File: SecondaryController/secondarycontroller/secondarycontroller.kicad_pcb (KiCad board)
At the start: 2 copper layers, 9 parts, among them J1 Receiver, J3 VIN, J4 APA102C, J5 I2C BUS, SW1 Calibrate, SW2 Reset

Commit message: Finished PCB Secondary
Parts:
- removed D1, D2: DIODE, Diode_THT:D_5W_P12.70mm_Horizontal
- added J2: Conn_01x07_Female, Connector_PinSocket_2.54mm:PinSocket_1x07_P2.54mm_Vertical, F.Cu at (175.3, 63.5)
- added XA1: Arduino_Uno_Shield, Arduino:Arduino_Uno_Shield, F.Cu at (144.9, 105.5)
- CF15: footprint Capacitor_THT:C_Rect_L41.5mm_W19.0mm_P37.50mm_MKS4 -> Capacitor_THT:C_Rect_L41.5mm_W13.0mm_P37.50mm_MKS4
- SW1, SW2: footprint Button_Switch_THT:SW_DIP_SPSTx01_Piano_10.8x4.1mm_W7.62mm_P2.54mm -> Button_Switch_THT:SW_PUSH_6mm
- moved J4 92.2 mm to (204.5, 71.1), turned to 180 degrees
- moved CF15 83.1 mm to (160.0, 94.0)
- moved SW2 67.2 mm to (147.3, 67.3)
- moved J5 58.4 mm to (149.9, 58.4), turned to 180 degrees
- moved J3 57.0 mm to (149.9, 94.0)
- moved J1 38.1 mm to (160.0, 72.4), turned to 180 degrees
- moved SW1 29.0 mm to (147.3, 78.7)
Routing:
- net Net-(CF15-Pad1): track 0.00 -> 156.2 mm
- net Net-(J2-Pad1): track 0.00 -> 72.0 mm
- net Net-(J3-Pad2): track 0.00 -> 47.4 mm
- net Net-(SW1-Pad1): track 0.00 -> 46.9 mm
- net Net-(SW2-Pad2): track 0.00 -> 41.1 mm
- net Net-(J4-Pad2): track 0.00 -> 25.5 mm
- net Net-(J1-Pad3): track 0.00 -> 22.3 mm
- net Net-(J5-Pad1): track 0.00 -> 21.0 mm
- net Net-(J4-Pad3): track 0.00 -> 20.1 mm
- net Net-(J5-Pad2): track 0.00 -> 17.0 mm
- net Net-(CF15-Pad2): track 0.00 -> 9.74 mm
- net Net-(J2-Pad3): track 0.00 -> 9.42 mm
- net Net-(J2-Pad4): track 0.00 -> 9.42 mm
- net Net-(J2-Pad5): track 0.00 -> 9.27 mm
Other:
- net class Default: trace_width 0.25 -> 1.5

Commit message: secondary as done
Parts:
- moved J1 12.9 mm to (172.1, 67.9), turned to 270 degrees
- moved J3 12.7 mm to (149.2, 81.3)
- moved SW2 9.86 mm to (156.8, 69.8)
- moved SW1 9.71 mm to (156.8, 80.6)
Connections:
- XA1 pad GND1: (no net) -> Net-(XA1-PadGND1)
- XA1 pad GND2: (no net) -> Net-(CF15-Pad1)
- XA1 pad GND3: (no net) -> Net-(XA1-PadGND3)
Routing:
- net Net-(CF15-Pad1): track 156.2 -> 223.5 mm
- net Net-(SW1-Pad1): track 46.9 -> 33.0 mm
- net Net-(J3-Pad2): track 47.4 -> 58.1 mm
- net Net-(SW2-Pad2): track 41.1 -> 34.6 mm
- net Net-(J1-Pad3): track 22.3 -> 17.1 mm
- net Net-(J5-Pad1): track 21.0 -> 19.1 mm
- net Net-(J5-Pad2): track 17.0 -> 15.5 mm
- added copper zone on B.Cu, net Net-(CF15-Pad1)
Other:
- board outline added: 69.2 x 59.1 mm

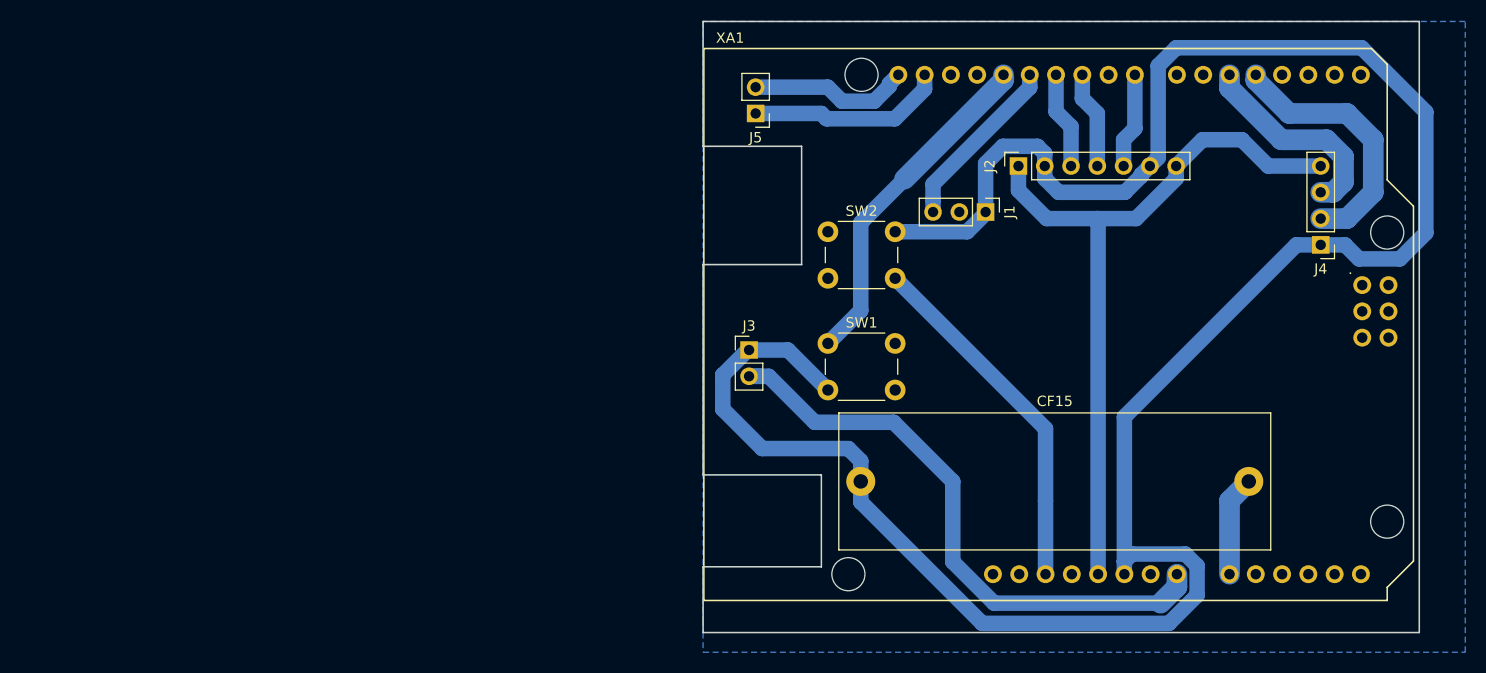
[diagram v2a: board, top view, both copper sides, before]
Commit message: new secondary controller pcb design
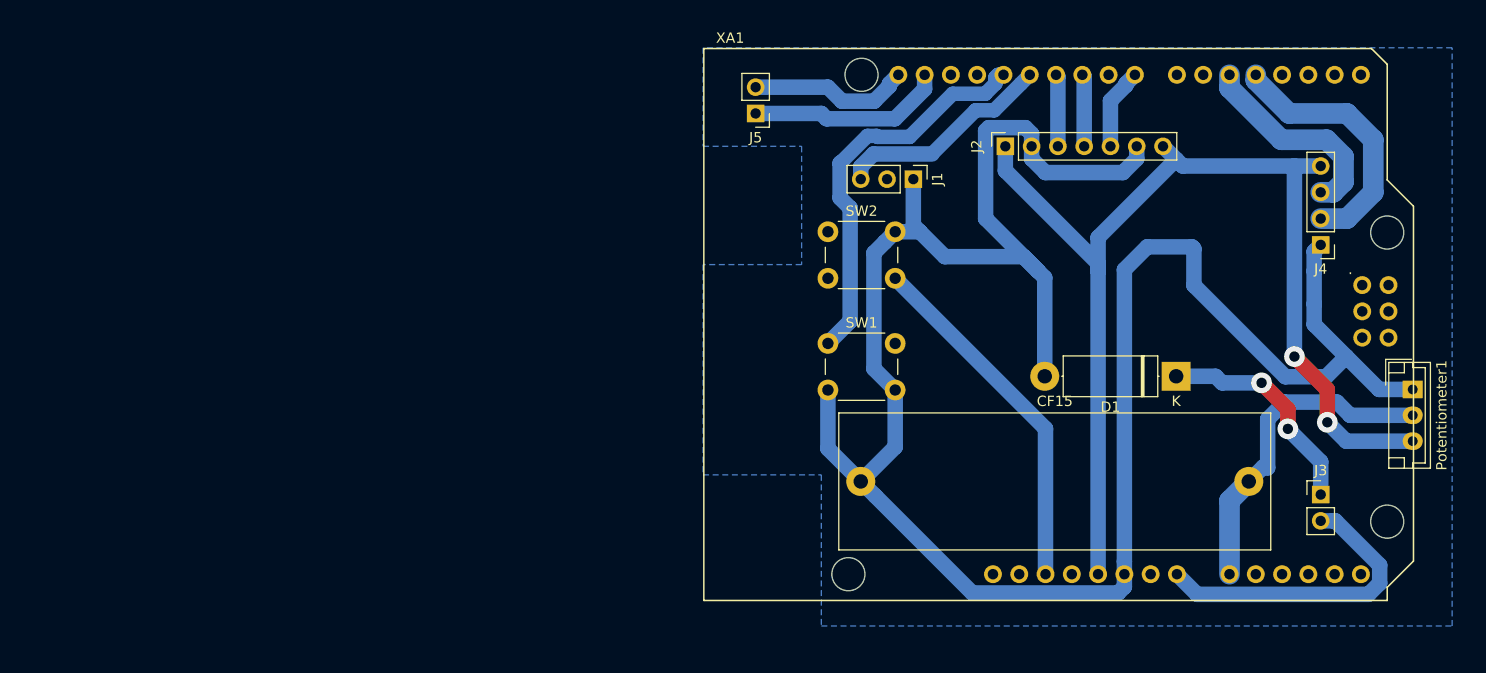
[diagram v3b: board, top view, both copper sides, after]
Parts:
- added D1: DIODE, Diode_THT:D_5W_P12.70mm_Horizontal, F.Cu at (190.5, 83.8)
- added Potentiometer1: Conn_01x03_Male, Connector_JST:JST_EH_B03B-EH-A_1x03_P2.50mm_Vertical, F.Cu at (213.4, 85.1)
- moved J3 57.0 mm to (204.5, 95.2)
- moved J1 7.67 mm to (165.1, 64.8)
- moved J2 2.29 mm to (174.0, 61.6)
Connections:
- J3 pad 1: Net-(CF15-Pad1) -> Net-(D1-Pad1)
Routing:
- net Net-(J2-Pad1): track 72.0 -> 110.8 mm, vias 0 -> 2
- net Net-(J3-Pad2): track 58.1 -> 30.1 mm
- net Net-(CF15-Pad2): track 9.74 -> 32.1 mm
- net Net-(D1-Pad1): track 0.00 -> 21.7 mm, vias 0 -> 2
- net Net-(CF15-Pad1): track 223.5 -> 215.2 mm
- net Net-(SW1-Pad1): track 33.0 -> 38.7 mm
- net Net-(J1-Pad3): track 17.1 -> 21.2 mm
- net Net-(J2-Pad3): track 9.42 -> 6.98 mm
- net Net-(J2-Pad4): track 9.42 -> 6.98 mm
- net Net-(J2-Pad5): track 9.27 -> 7.89 mm
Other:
- board outline removed
- net class Default: clearance 0.2 -> 0.3
- rule trace_clearance: 0.2 -> 0.3

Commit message: secondary better pcb design
Signed-off-by: Kai Boernert <kai-boernert@visiongamestudios.de>
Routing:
- net (no net): track 0.00 -> 50.0 mm
- net Net-(CF15-Pad1): track 215.2 -> 237.8 mm
- net Net-(J2-Pad1): track 110.8 -> 132.3 mm
- net Net-(SW1-Pad1): track 38.7 -> 59.4 mm
- net Net-(SW2-Pad2): track 34.6 -> 48.6 mm
- net Net-(CF15-Pad2): track 32.1 -> 42.1 mm
- net Net-(J3-Pad2): track 30.1 -> 33.1 mm
- net Net-(XA1-PadGND3): track 0.00 -> 2.54 mm
- net Net-(XA1-PadA3): track 0.00 -> 2.54 mm
- net Net-(XA1-PadA2): track 0.00 -> 2.54 mm
- net Net-(XA1-PadA1): track 0.00 -> 2.54 mm
- net Net-(XA1-PadD7): track 0.00 -> 2.50 mm
- net Net-(XA1-PadA4): track 0.00 -> 2.48 mm
- net Net-(XA1-PadD0): track 0.00 -> 2.39 mm
- net Net-(XA1-PadD6): track 0.00 -> 2.39 mm
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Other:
- net class Default: clearance 0.3 -> 0.1; trace_width 1.5 -> 1
- rule trace_clearance: 0.3 -> 0.1

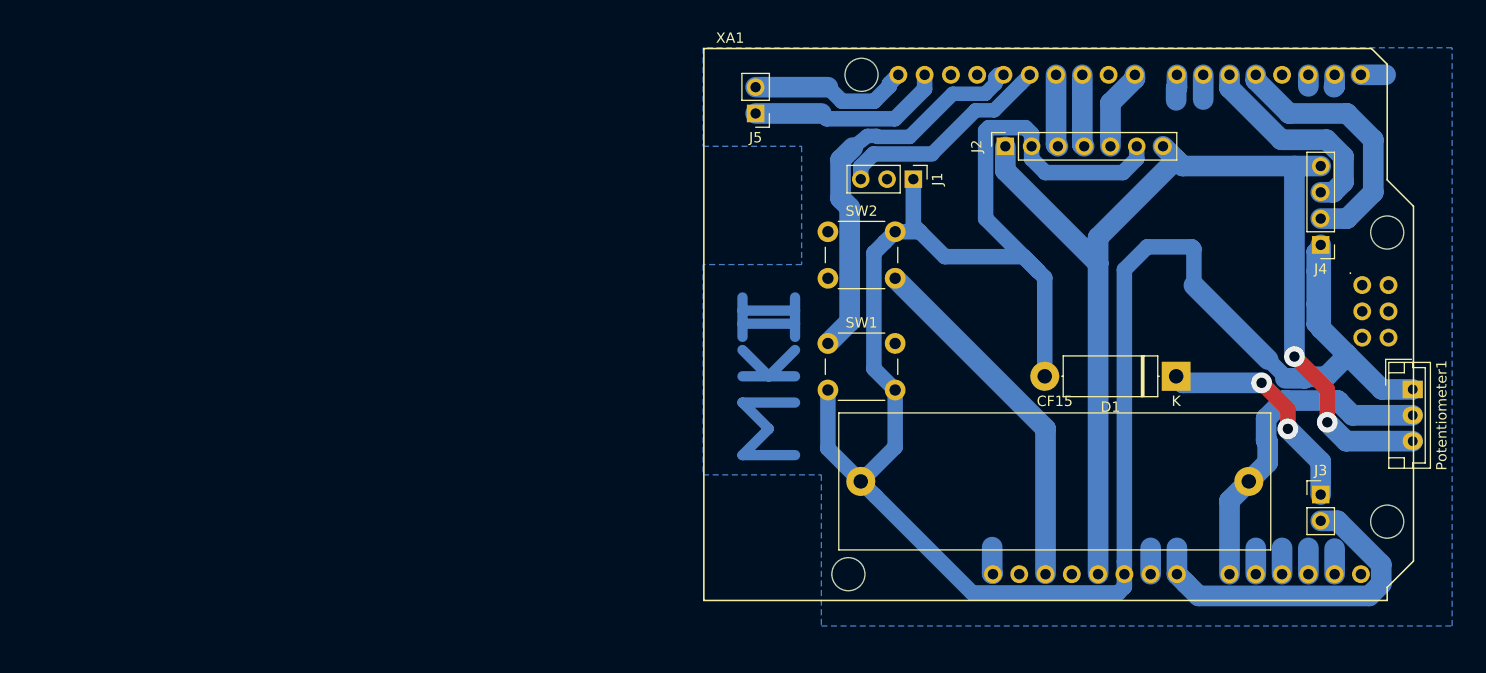
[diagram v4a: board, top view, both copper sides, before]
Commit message: secondary controller mk2
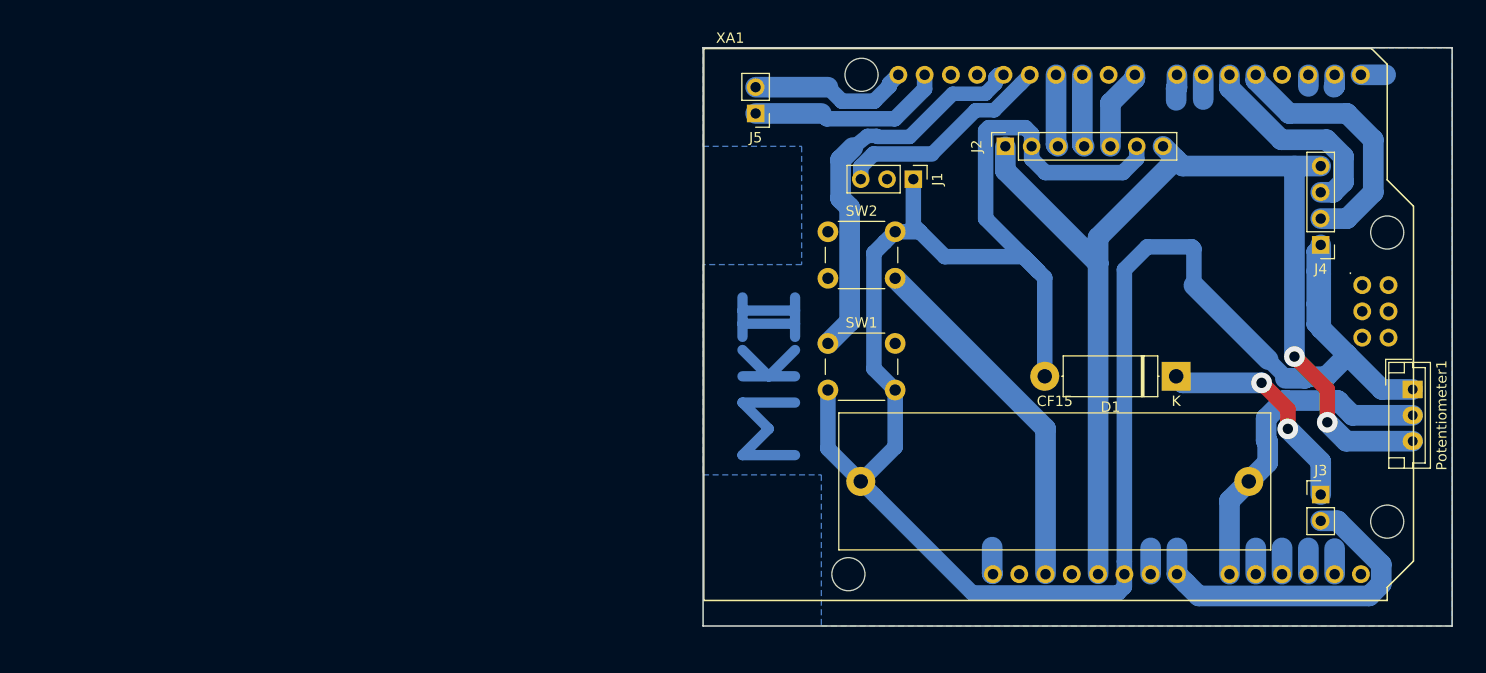
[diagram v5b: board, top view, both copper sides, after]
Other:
- board outline added: 72.4 x 55.9 mm
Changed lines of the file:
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@@
-(kicad_pcb (version 20171130) (host pcbnew 5.0.0)
+(kicad_pcb (version 20171130) (host pcbnew "(5.0.0)")
   (general
     (thickness 1.6)
-    (drawings 0)
+    (drawings 1)
     (tracks 206)
     (zones 0)
@@
     )
   )
+  (gr_poly (pts (xy 217.17 107.95) (xy 144.78 107.95) (xy 144.78 52.07) (xy 217.17 52.07)) (layer Edge.Cuts) (width 0.15))
   (segment (start 172.72 102.87) (end 172.758592 102.908592) (width 2) (layer B.Cu) (net 0))
   (segment (start 172.72 100.33) (end 172.72 102.87) (width 2) (layer B.Cu) (net 0))
